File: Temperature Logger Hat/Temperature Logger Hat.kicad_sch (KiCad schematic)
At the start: 18 parts, among them J1 GPIO, J2 SPI, J3 1-wire, J4 Jumper_Mode, SW1 SW_Power_Off, SW2 SW_Mode2, U1 CAT24C256

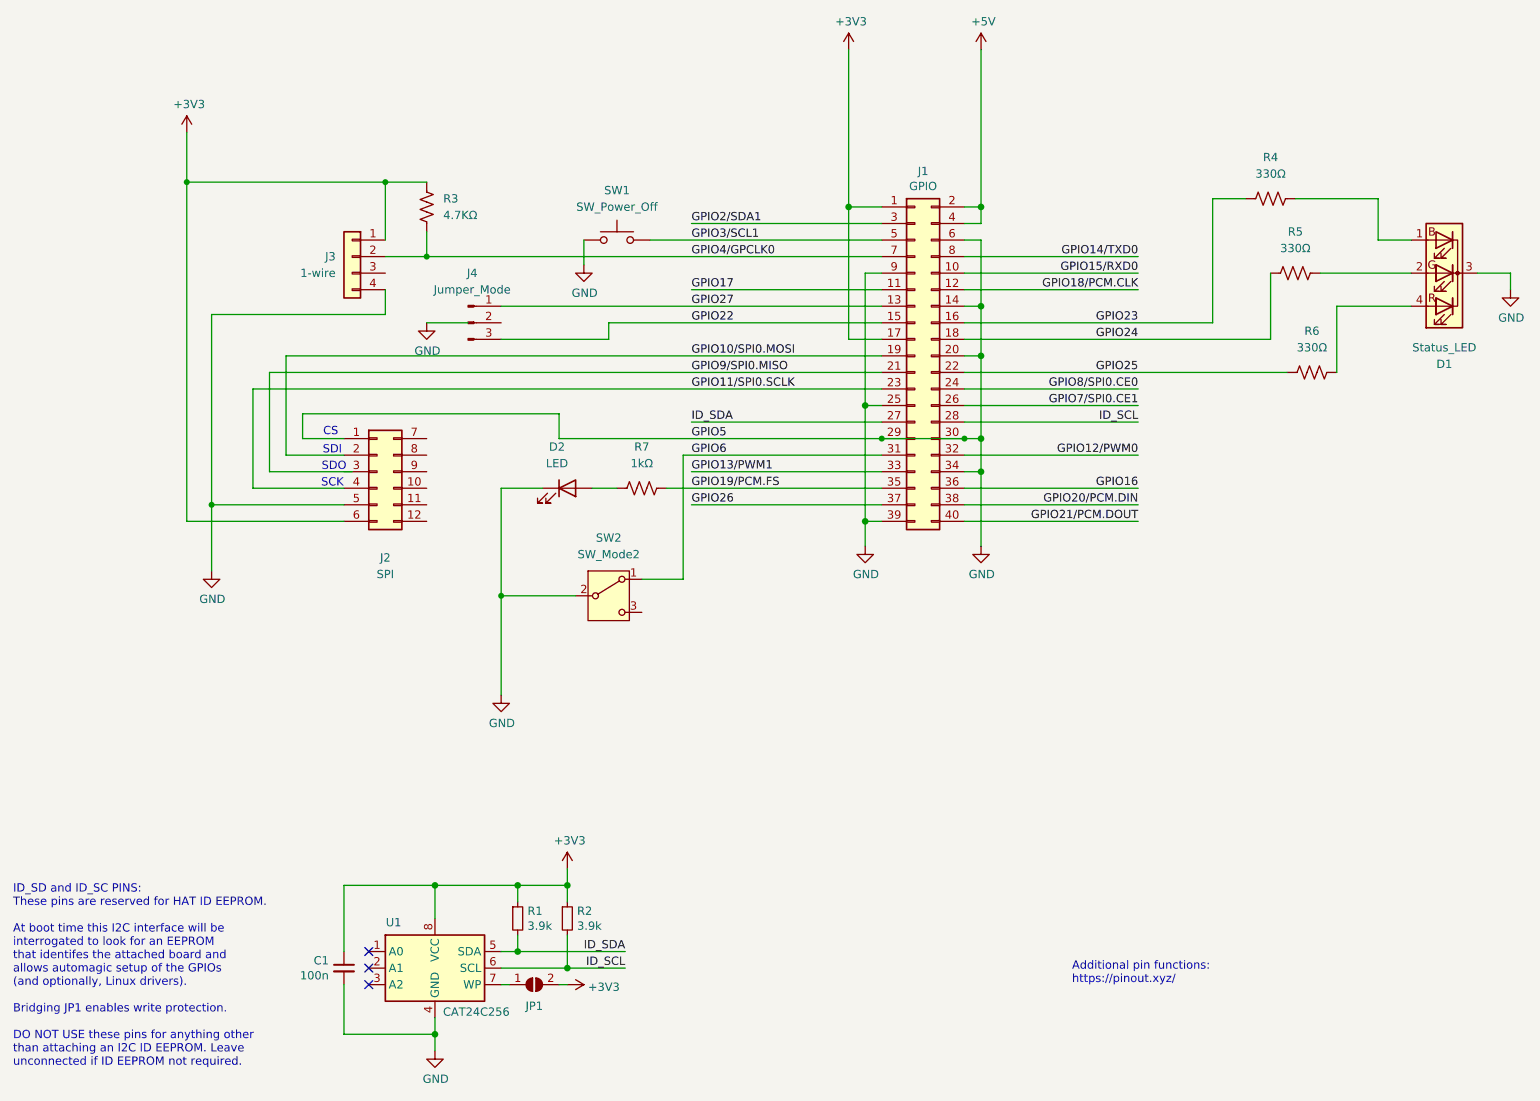
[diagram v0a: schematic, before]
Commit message: Update schematic for Hat
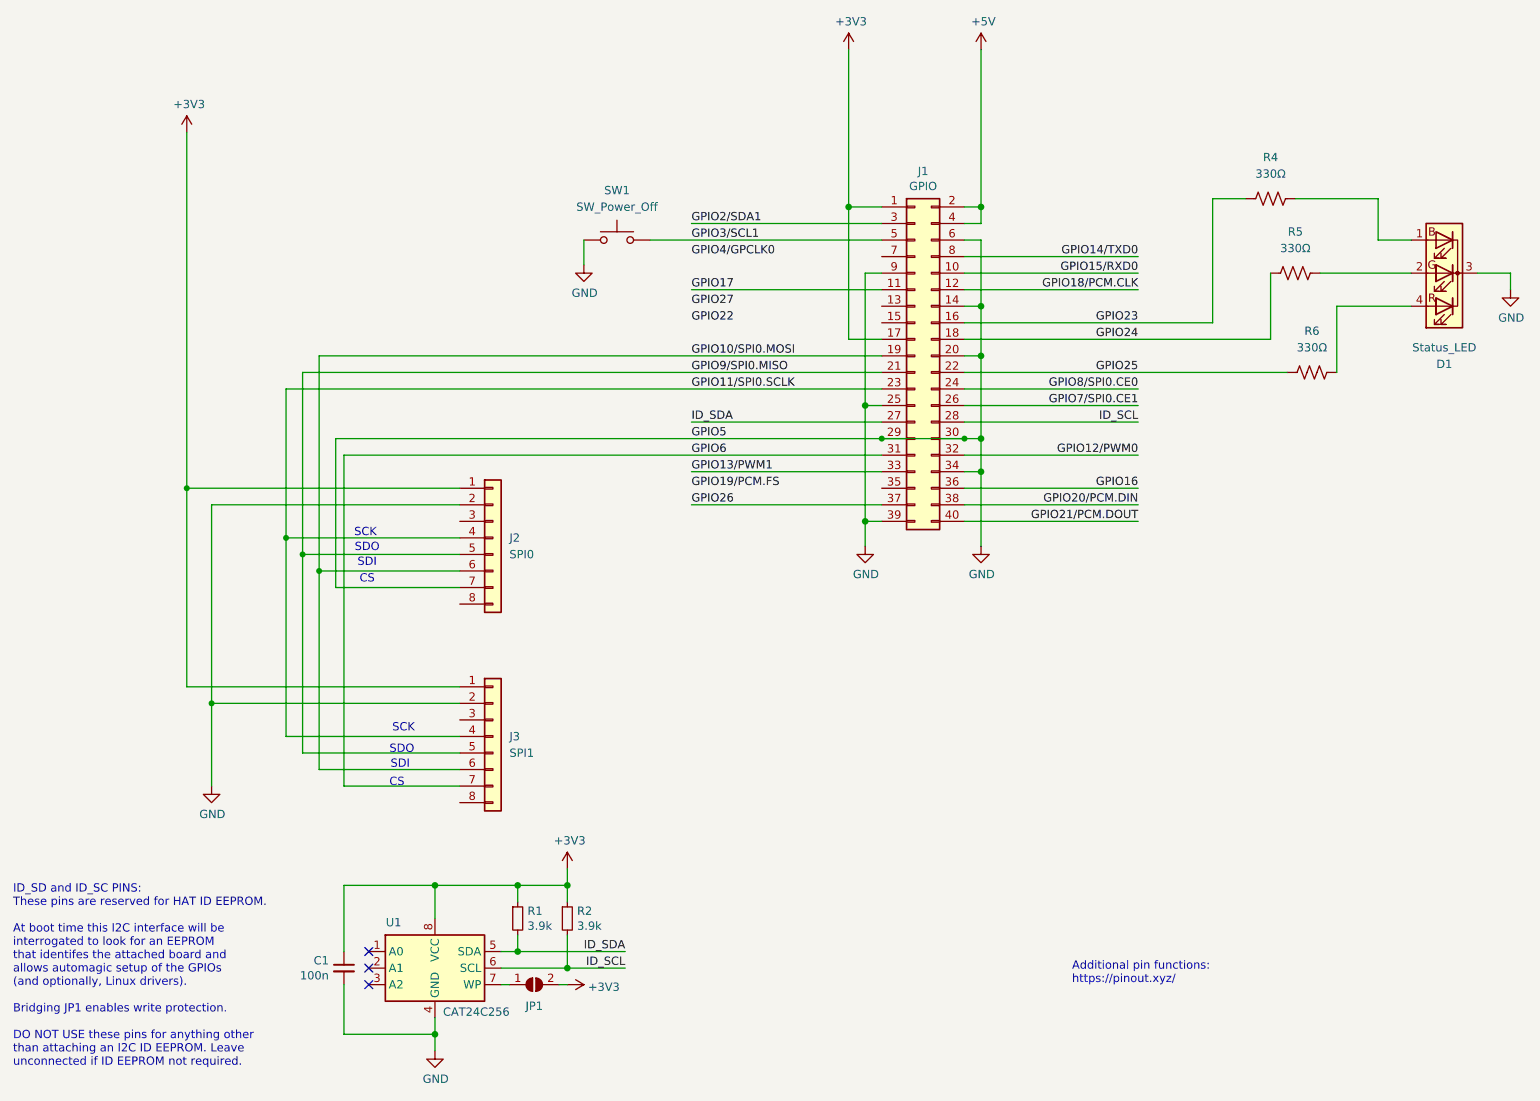
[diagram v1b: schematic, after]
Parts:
- removed D2: LED, symbol Device:LED
- removed J2: SPI, symbol Connector_Generic:Conn_02x06_Top_Bottom
- removed J3: 1-wire, symbol Connector_Generic:Conn_01x04
- removed J4: Jumper_Mode, symbol Connector:Conn_01x03_Pin
- removed R3: 4.7KΩ, symbol Device:R_US
- removed R7: 1kΩ, symbol Device:R_US
- removed SW2: SW_Mode2, symbol Switch:SW_SPDT
- added J2: SPI0, symbol Connector_Generic:Conn_01x08
- added J3: SPI1, symbol Connector_Generic:Conn_01x08
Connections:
- net +3V3: now also J2.1 (Pin_1), J3.1 (Pin_1)
- net GND: now also J2.2 (Pin_2), J2.7 (Pin_7), J3.2 (Pin_2)
- net GPIO10/SPI0.MOSI: now also J2.6 (Pin_6), J3.6 (Pin_6)
- net GPIO11/SPI0.SCLK: now also J2.4 (Pin_4), J3.4 (Pin_4)
- net GPIO19/PCM.FS: no longer J1.35 (Pin_35)
- net GPIO22: no longer J1.15 (Pin_15)
- net GPIO27: no longer J1.13 (Pin_13)
- net GPIO4/GPCLK0: no longer J1.7 (Pin_7)
- net GPIO6: now also J3.7 (Pin_7)
- net GPIO9/SPI0.MISO: now also J2.5 (Pin_5), J3.5 (Pin_5)
